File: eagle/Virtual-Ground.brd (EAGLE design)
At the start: 100 x 80 mm, 8 parts

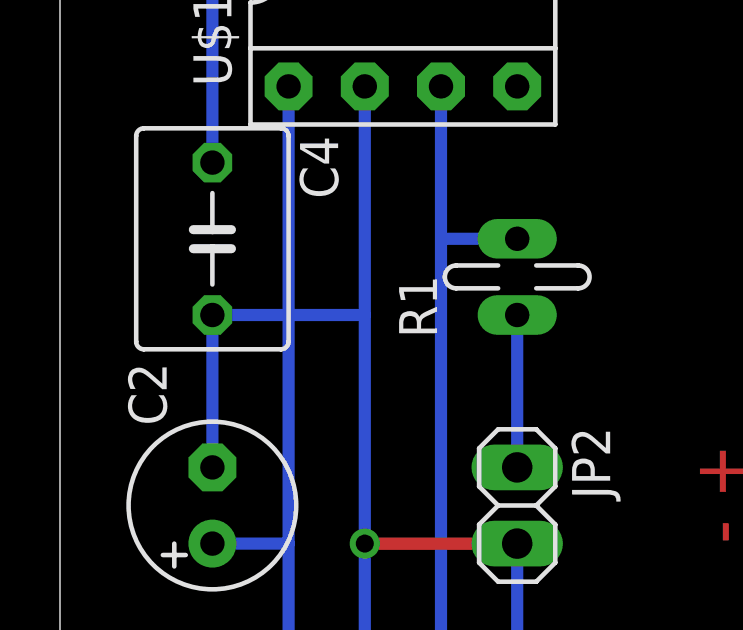
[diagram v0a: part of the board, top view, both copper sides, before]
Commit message: 仮想グランド基板設計図修正
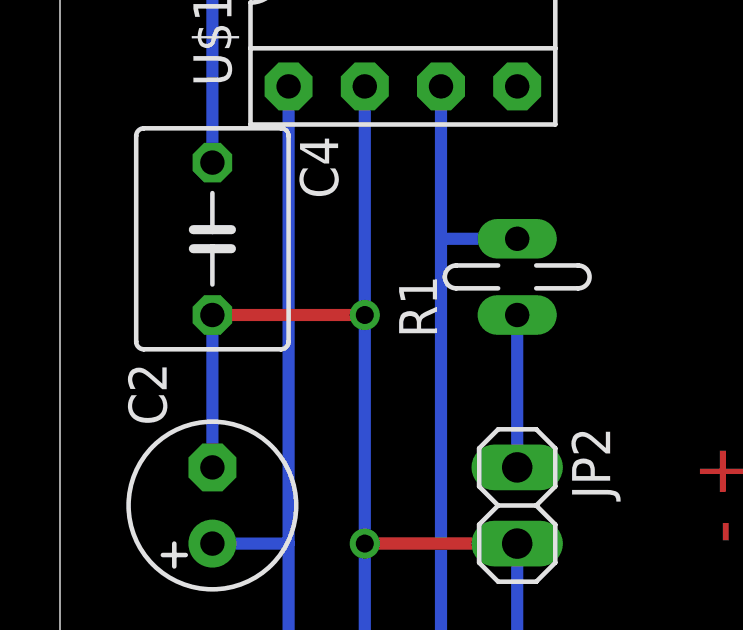
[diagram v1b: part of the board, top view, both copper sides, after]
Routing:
- net V-: vias 1 -> 2
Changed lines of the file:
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@@
 <layer number="98" name="Guide" color="6" fill="1" visible="no" active="no"/>
 <layer number="100" name="Grid" color="7" fill="1" visible="yes" active="yes"/>
+<layer number="101" name="Grid2" color="7" fill="1" visible="no" active="yes"/>
 </layers>
 <board>
@@
 <wire x1="0" y1="58.42" x2="0" y2="71.12" width="0" layer="100"/>
 <wire x1="0" y1="71.12" x2="0" y2="78.74" width="0" layer="100"/>
-<wire x1="7.62" y1="78.74" x2="7.62" y2="33.02" width="0" layer="100" style="shortdash"/>
 <wire x1="0" y1="71.12" x2="17.78" y2="71.12" width="0" layer="100" style="shortdash"/>
 <wire x1="0" y1="58.42" x2="17.78" y2="58.42" width="0" layer="100" style="shortdash"/>
@@
 <text x="22.86" y="40.64" size="1.778" layer="1" rot="R90">GND + -</text>
 <text x="22.86" y="53.34" size="1.778" layer="1" rot="R90">- +</text>
+<wire x1="2.54" y1="80.01" x2="2.54" y2="33.02" width="0" layer="101"/>
+<wire x1="2.54" y1="33.02" x2="5.08" y2="33.02" width="0" layer="101"/>
+<wire x1="5.08" y1="33.02" x2="5.08" y2="80.01" width="0" layer="101"/>
+<wire x1="5.08" y1="80.01" x2="7.62" y2="80.01" width="0" layer="101"/>
+<wire x1="10.16" y1="80.01" x2="10.16" y2="33.02" width="0" layer="101"/>
+<wire x1="12.7" y1="80.01" x2="12.7" y2="33.02" width="0" layer="101"/>
+<wire x1="15.24" y1="80.01" x2="15.24" y2="33.02" width="0" layer="101"/>
+<wire x1="0" y1="78.74" x2="17.78" y2="78.74" width="0" layer="101"/>
+<wire x1="17.78" y1="76.2" x2="0" y2="76.2" width="0" layer="101"/>
+<wire x1="0" y1="73.66" x2="17.78" y2="73.66" width="0" layer="101"/>
+<wire x1="17.78" y1="68.58" x2="0" y2="68.58" width="0" layer="101"/>
+<wire x1="0" y1="63.5" x2="17.78" y2="63.5" width="0" layer="101"/>
+<wire x1="17.78" y1="60.96" x2="0" y2="60.96" width="0" layer="101"/>
+<wire x1="0" y1="55.88" x2="17.78" y2="55.88" width="0" layer="101"/>
+<wire x1="0" y1="53.34" x2="17.78" y2="53.34" width="0" layer="101"/>
+<wire x1="0" y1="50.8" x2="17.78" y2="50.8" width="0" layer="101"/>
+<wire x1="0" y1="48.26" x2="17.78" y2="48.26" width="0" layer="101"/>
+<wire x1="0" y1="43.18" x2="17.78" y2="43.18" width="0" layer="101"/>
+<wire x1="0" y1="40.64" x2="17.78" y2="40.64" width="0" layer="101"/>
+<wire x1="0" y1="38.1" x2="17.78" y2="38.1" width="0" layer="101"/>
+<wire x1="0" y1="35.56" x2="17.78" y2="35.56" width="0" layer="101"/>
+<wire x1="0" y1="66.04" x2="17.78" y2="66.04" width="0" layer="101"/>
 </plain>
 <attributes>
@@
 <contactref element="JP2" pad="2"/>
 <contactref element="JP1" pad="3"/>
+<wire x1="10.16" y1="68.58" x2="10.16" y2="60.96" width="0" layer="19" extent="1-16"/>
 <wire x1="10.16" y1="68.58" x2="10.16" y2="60.96" width="0.4064" layer="16"/>
 <wire x1="10.16" y1="60.96" x2="10.16" y2="53.34" width="0.4064" layer="16"/>
@@
 <wire x1="10.16" y1="40.64" x2="5.08" y2="40.64" width="0.4064" layer="16"/>
 <wire x1="15.24" y1="53.34" x2="15.24" y2="48.26" width="0.4064" layer="16"/>
-<wire x1="5.08" y1="60.96" x2="10.16" y2="60.96" width="0.4064" layer="16"/>
 <wire x1="5.08" y1="55.88" x2="5.08" y2="60.96" width="0.4064" layer="16"/>
 <via x="10.16" y="53.34" extent="1-16" drill="0.6" shape="square"/>
 <wire x1="15.24" y1="53.34" x2="10.16" y2="53.34" width="0.4064" layer="1"/>
+<via x="10.16" y="60.96" extent="1-16" drill="0.6" shape="square"/>
+<wire x1="5.08" y1="60.96" x2="10.16" y2="60.96" width="0.4064" layer="1"/>
 </signal>
 <signal name="V+IN">
